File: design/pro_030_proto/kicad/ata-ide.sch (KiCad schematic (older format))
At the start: 31 parts, among them J1 Conn_02x32_Odd_Even, J2 Conn_02x20_Odd_Even, J3 Conn_02x22_Odd_Even, Q1 2N2907, U1 16V8, U2 ATF750, U3 74HCT241, U4 74HCT245, U5 74HCT245

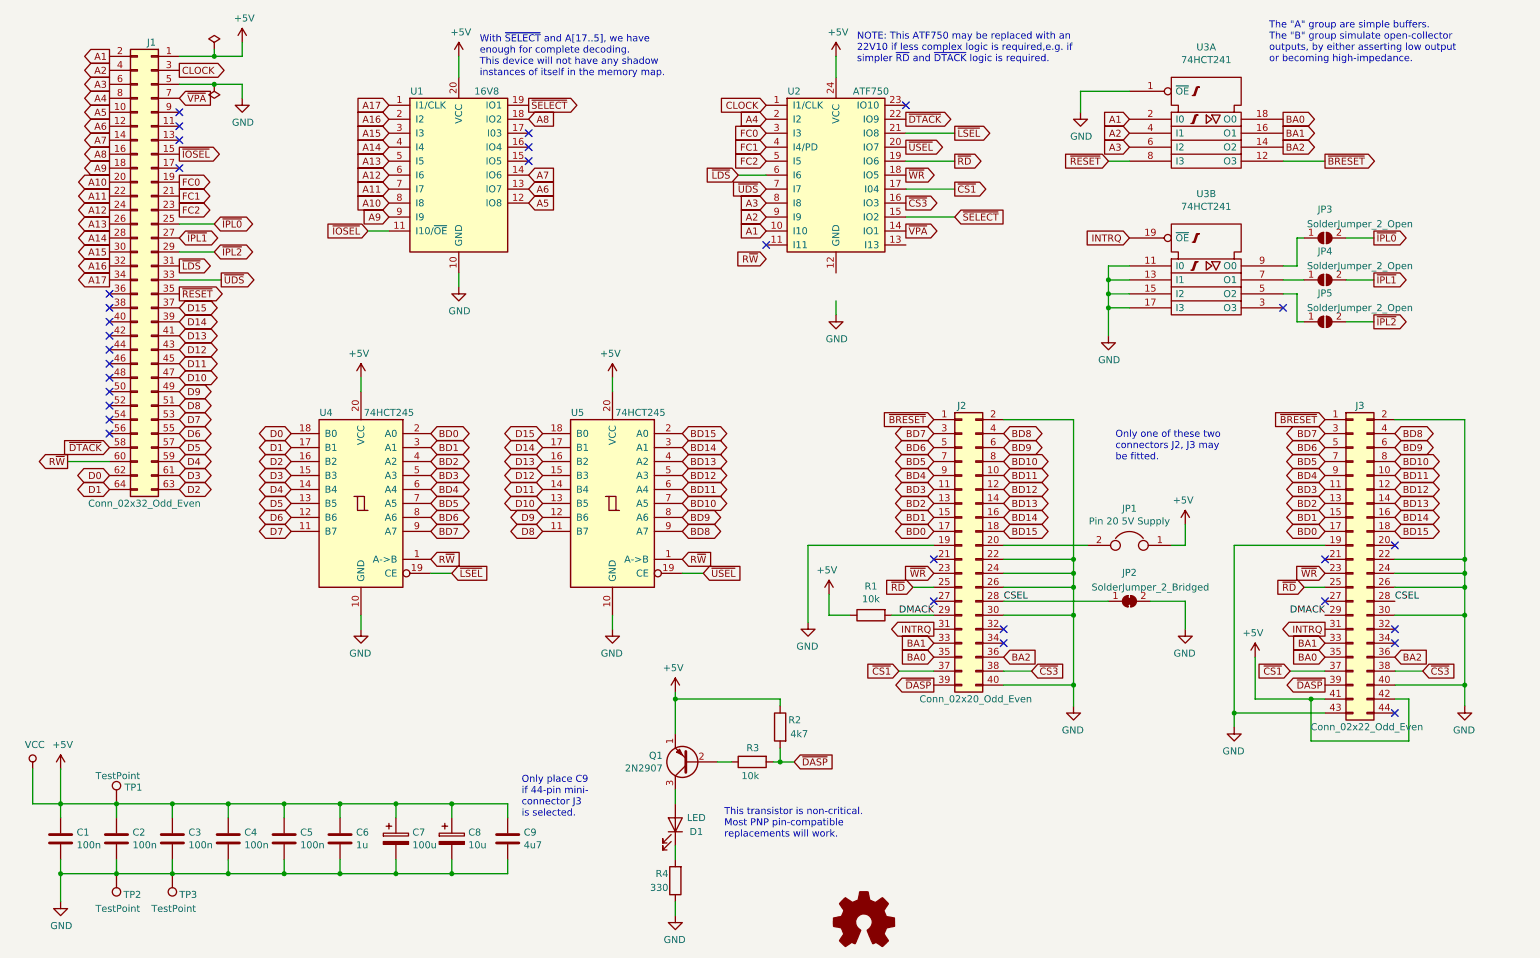
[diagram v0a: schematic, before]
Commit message: Layout for ATA, plus fixes
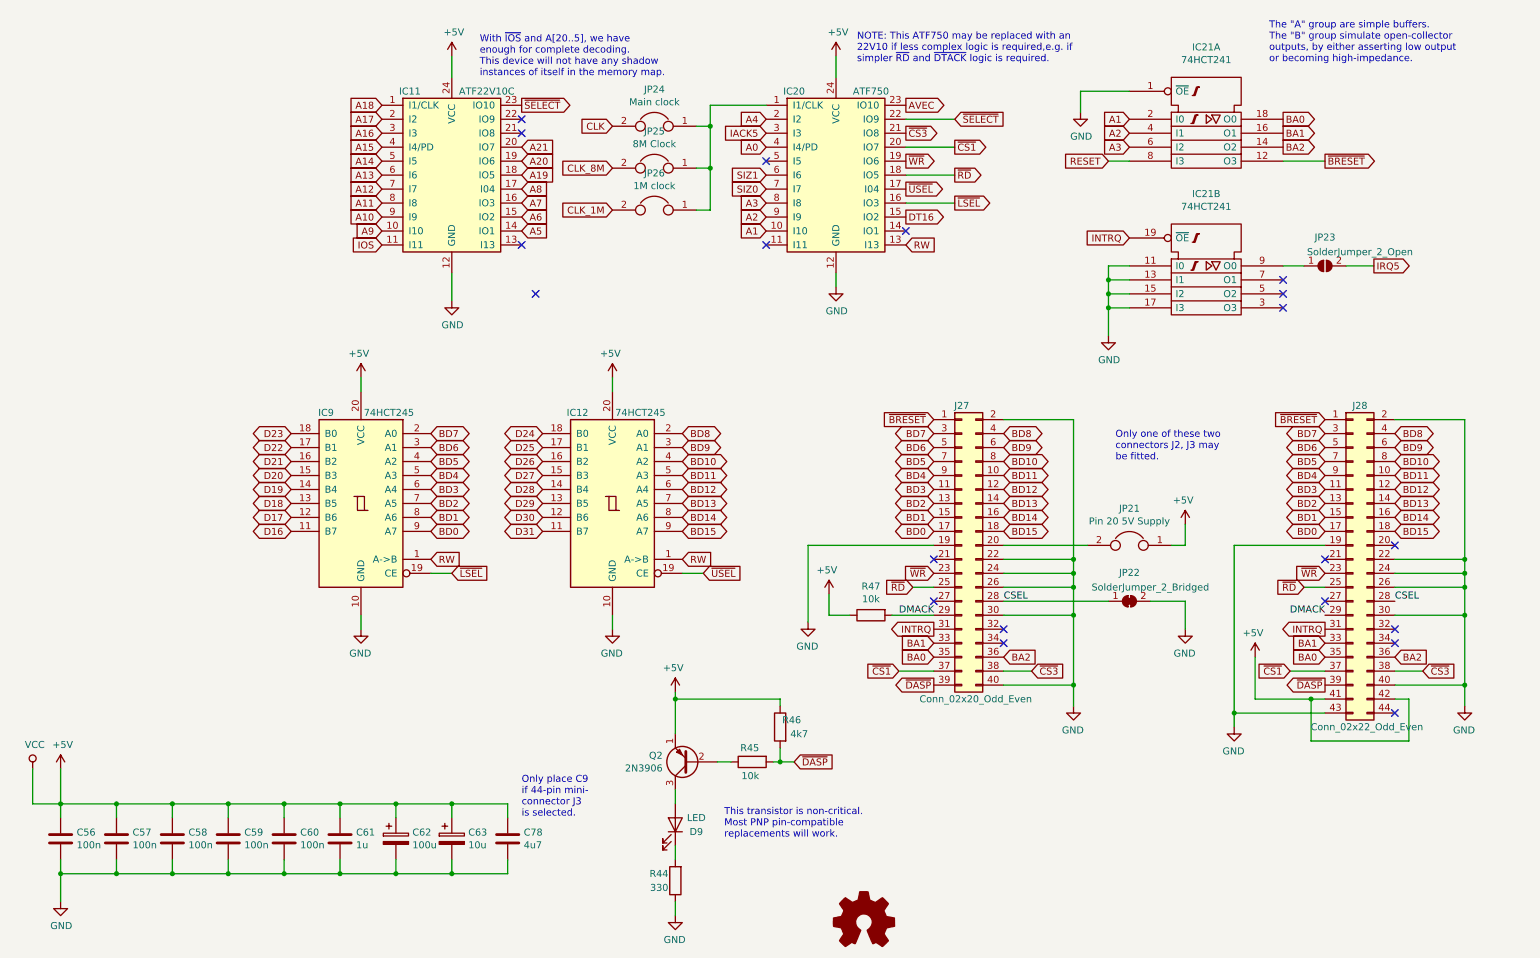
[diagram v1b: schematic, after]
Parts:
- removed J1: Conn_02x32_Odd_Even, Connector_PinHeader_2.54mm:PinHeader_2x32_P2.54mm_Vertical, symbol Connector_Generic:Conn_02x32_Odd_Even
- removed JP4, JP5: SolderJumper_2_Open, Jumper:SolderJumper-2_P1.3mm_Open_Pad1.0x1.5mm, symbol Jumper:SolderJumper_2_Open
- removed TP1, TP2, TP3: TestPoint, Measurement_Points:Measurement_Point_Round-TH_Big, symbol Connector:TestPoint
- removed U1: 16V8, Housings_DIP:DIP-20_W7.62mm_Socket_LongPads, symbol Logic_Programmable:GAL16V8
- added IC11: ATF22V10C, Package_DIP:DIP-24_W7.62mm_Socket_LongPads, symbol rosco_m68k:GAL22V10
- added JP24: Main clock, Connector_PinHeader_2.54mm:PinHeader_1x02_P2.54mm_Vertical, symbol Device:Jumper
- added JP25: 8M Clock, Connector_PinHeader_2.54mm:PinHeader_1x02_P2.54mm_Vertical, symbol Device:Jumper
- added JP26: 1M clock, Connector_PinHeader_2.54mm:PinHeader_1x02_P2.54mm_Vertical, symbol Device:Jumper
- C56: renamed from C1; footprint Capacitors_THT:C_Rect_L4.0mm_W2.5mm_P2.50mm -> Capacitor_THT:C_Rect_L4.0mm_W2.5mm_P2.50mm
- C57: renamed from C2; footprint Capacitors_THT:C_Rect_L4.0mm_W2.5mm_P2.50mm -> Capacitor_THT:C_Rect_L4.0mm_W2.5mm_P2.50mm
- C58: renamed from C3; footprint Capacitors_THT:C_Rect_L4.0mm_W2.5mm_P2.50mm -> Capacitor_THT:C_Rect_L4.0mm_W2.5mm_P2.50mm
- C59: renamed from C4; footprint Capacitors_THT:C_Rect_L4.0mm_W2.5mm_P2.50mm -> Capacitor_THT:C_Rect_L4.0mm_W2.5mm_P2.50mm
- C60: renamed from C5; footprint Capacitors_THT:C_Rect_L4.0mm_W2.5mm_P2.50mm -> Capacitor_THT:C_Rect_L4.0mm_W2.5mm_P2.50mm
- C61: renamed from C6; footprint Capacitors_THT:C_Rect_L7.0mm_W4.5mm_P5.00mm -> Capacitor_THT:C_Rect_L7.0mm_W4.5mm_P5.00mm
- C62: renamed from C7; footprint Capacitors_THT:CP_Radial_D8.0mm_P2.50mm -> Capacitor_THT:CP_Radial_D8.0mm_P2.50mm
- C63: renamed from C8; footprint Capacitors_THT:CP_Radial_D8.0mm_P2.50mm -> Capacitor_THT:CP_Radial_D8.0mm_P2.50mm
- C78: renamed from C9; footprint Capacitors_THT:C_Rect_L7.0mm_W4.5mm_P5.00mm -> Capacitor_THT:C_Rect_L7.0mm_W4.5mm_P5.00mm
- D9: renamed from D1; footprint LEDs:LED_D5.0mm -> LED_THT:LED_D3.0mm
- JP21: renamed from JP1; footprint Connector_PinHeader_2.00mm:PinHeader_1x02_P2.00mm_Vertical -> Connector_PinHeader_2.54mm:PinHeader_1x02_P2.54mm_Vertical
- Q2: renamed from Q1; value 2N2907 -> 2N3906; footprint Package_TO_SOT_THT:TO-18-3 -> Package_TO_SOT_THT:TO-92_HandSolder
- R44: renamed from R4; footprint Resistors_THT:R_Axial_DIN0207_L6.3mm_D2.5mm_P10.16mm_Horizontal -> rosco_m68k:R-0207_10
- R45: renamed from R3; footprint Resistors_THT:R_Axial_DIN0207_L6.3mm_D2.5mm_P10.16mm_Horizontal -> rosco_m68k:R-0207_10
- R46: renamed from R2; footprint Resistors_THT:R_Axial_DIN0207_L6.3mm_D2.5mm_P10.16mm_Horizontal -> rosco_m68k:R-0207_10
- R47: renamed from R1; footprint Resistors_THT:R_Axial_DIN0207_L6.3mm_D2.5mm_P10.16mm_Horizontal -> rosco_m68k:R-0207_10
- renumbered U5 to IC12, U2 to IC20, U3 to IC21, U4 to IC9, J2 to J27, J3 to J28, JP2 to JP22, JP3 to JP23
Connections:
- net R~W~ is gone; now on net RW: IC12.1 (A->B), IC9.1 (A->B)
- net ~DTACK~ is gone; now on net ~SELECT~: IC20.22 (IO9)
- net +5V: now also IC11.24 (VCC)
- net A10: now also IC11.9 (I9)
- net A11: now also IC11.8 (I8)
- net A12: now also IC11.7 (I7)
- net A13: now also IC11.6 (I6)
- net A14: now also IC11.5 (I5)
- net A15: now also IC11.4 (I4/PD)
- net A16: now also IC11.3 (I3)
- net A17: now also IC11.2 (I2)
- net A5: now also IC11.14 (IO1)
- net A6: now also IC11.15 (IO2)
- net A7: now also IC11.16 (IO3)
- net A8: now also IC11.17 (I04)
- net A9: now also IC11.10 (I10)
- net BD0: now also IC9.9 (A7); no longer IC9.2 (A0)
- net BD1: now also IC9.8 (A6); no longer IC9.3 (A1)
- net BD10: now also IC12.4 (A2); no longer IC12.7 (A5)
- net BD11: now also IC12.5 (A3); no longer IC12.6 (A4)
- net BD12: now also IC12.6 (A4); no longer IC12.5 (A3)
- net BD13: now also IC12.7 (A5); no longer IC12.4 (A2)
- net BD14: now also IC12.8 (A6); no longer IC12.3 (A1)
- net BD15: now also IC12.9 (A7); no longer IC12.2 (A0)
- net BD2: now also IC9.7 (A5); no longer IC9.4 (A2)
- net BD3: now also IC9.6 (A4); no longer IC9.5 (A3)
- net BD4: now also IC9.5 (A3); no longer IC9.6 (A4)
- net BD5: now also IC9.4 (A2); no longer IC9.7 (A5)
- net BD6: now also IC9.3 (A1); no longer IC9.8 (A6)
- net BD7: now also IC9.2 (A0); no longer IC9.9 (A7)
- net BD8: now also IC12.2 (A0); no longer IC12.9 (A7)
- net BD9: now also IC12.3 (A1); no longer IC12.8 (A6)
- net GND: now also IC20.12 (GND), IC11.12 (GND)
- net ~CS1~: now also IC20.20 (IO7); no longer IC20.17 (I04)
- net ~CS3~: now also IC20.21 (IO8); no longer IC20.16 (IO3)
- net ~LSEL~: now also IC20.16 (IO3); no longer IC20.21 (IO8)
- net ~RD~: now also IC20.18 (IO5); no longer IC20.19 (IO6)
- net ~SELECT~: now also IC11.23 (IO10); no longer IC20.15 (IO2)
- net ~USEL~: now also IC20.17 (I04); no longer IC20.20 (IO7)
- net ~WR~: now also IC20.19 (IO6); no longer IC20.18 (IO5)
- net RW: now reaches IC20.13 (I13)
- net AVEC: now reaches IC20.23 (IO10)
- net CLOCK: no longer names the net of IC20.1 (I1/CLK)
- net CLOCK: now also JP24.1, JP25.1, JP26.1
- net D0 renamed D23
- net D1 renamed D22
- net D10 renamed D29
- net D11 renamed D28
- net D12 renamed D27
- net D13 renamed D26
- net D14 renamed D25
- net D15 renamed D24
- net D2 renamed D21
- net D3 renamed D20
- net D4 renamed D19
- net D5 renamed D18
- net D6 renamed D17
- net D7 renamed D16
- net D8 renamed D31
- net D9 renamed D30
- net FC0 renamed IACK5
- net FC1 renamed A0
- net FC2: no longer names the net of IC20.5 (I5)
- net ~IPL0~ renamed IRQ5
- net ~LDS~ renamed SIZ1
- net ~RESET~ renamed RESET
- net ~UDS~ renamed SIZ0
- net ~VPA~: no longer names the net of IC20.14 (IO1)
- new net A18: IC11.1 (I1/CLK)
- new net A19: IC11.18 (IO5)
- new net A20: IC11.19 (IO6)
- new net A21: IC11.20 (IO7)
- new net CLK: JP24.2
- new net CLK_1M: JP26.2
- new net CLK_8M: JP25.2
- new net DT16: IC20.15 (IO2)
- new net IOS: IC11.11 (I11)
- no-connect marks 31 -> 20
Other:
- note added: "With ~IOS~ and A[20..5], we have\nenough for complete decoding.\nThis device will not have any shadow\ninstances of itself in the memory map."
- note removed: "With ~SELECT~ and A[17..5], we have\nenough for complete decoding.\nThis device will not have any shadow\ninstances of itself in the memory map."
- moved on the sheet: JP23

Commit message: Tidy up a bit
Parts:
- JP23: footprint Jumper:SolderJumper-2_P1.3mm_Open_Pad1.0x1.5mm -> Jumper:SolderJumper-2_P1.3mm_Bridged_Pad1.0x1.5mm; symbol Jumper:SolderJumper_2_Open -> Jumper:SolderJumper_2_Bridged
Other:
- note added: "Only place C78\nif 44-pin mini-\nconnector J3\nis selected."
- note removed: "Only place C9\nif 44-pin mini-\nconnector J3\nis selected."
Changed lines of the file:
@@
 	650  6650 850  6650
 $Comp
-L Jumper:SolderJumper_2_Open JP23
+L Jumper:SolderJumper_2_Bridged JP23
 U 1 1 6064DE34
 P 9900 2800
 F 0 "JP23" H 9900 3005 50  0000 C CNN
 F 1 "SolderJumper_2_Open" H 10150 2900 50  0000 C CNN
-F 2 "Jumper:SolderJumper-2_P1.3mm_Open_Pad1.0x1.5mm" H 9900 2800 50  0001 C CNN
+F 2 "Jumper:SolderJumper-2_P1.3mm_Bridged_Pad1.0x1.5mm" H 9900 2800 50  0001 C CNN
 F 3 "~" H 9900 2800 50  0001 C CNN
 	1    9900 2800
@@
 Connection ~ 3650 7150
 Text Notes 4150 6750 0    50   ~ 0
-Only place C9\nif 44-pin mini-\nconnector J3\nis selected.
+Only place C78\nif 44-pin mini-\nconnector J3\nis selected.
 Wire Wire Line
 	6900 2350 7250 2350

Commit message: Add panel header block
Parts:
- added J26: IDE_LED, Connector_PinHeader_2.54mm:PinHeader_2x01_P2.54mm_Vertical, symbol Connector_Generic:Conn_02x01
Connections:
- net at D9.1 (K), R44.2: now also J26.2 (Pin_2)
- net at D9.2 (A), Q2.3 (C): now also J26.1 (Pin_1)
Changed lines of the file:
@@
 	4050 7150 3650 7150
 Connection ~ 3650 7150
-Text Notes 4150 6750 0    50   ~ 0
+Text Notes 3550 6450 0    50   ~ 0
 Only place C78\nif 44-pin mini-\nconnector J3\nis selected.
 Wire Wire Line
@@
 NoConn ~ 4150 2650
 NoConn ~ 4250 3000
+$Comp
+L Connector_Generic:Conn_02x01 J?
+U 1 1 61E8C30F
+P 4800 6750
+AR Path="/60FC48A0/61E8C30F" Ref="J?"  Part="1"
+AR Path="/61B3F22F/61E8C30F" Ref="J26"  Part="1"
+F 0 "J26" H 4850 6967 50  0000 C CNN
+F 1 "IDE_LED" H 4850 6876 50  0000 C CNN
+F 2 "Connector_PinHeader_2.54mm:PinHeader_2x01_P2.54mm_Vertical" H 4800 6750 50  0001 C CNN
+F 3 "~" H 4800 6750 50  0001 C CNN
+	1    4800 6750
+	0    1    1    0
+$EndComp
+Wire Wire Line
+	4800 7050 5250 7050
+Connection ~ 5250 7050
+Wire Wire Line
+	4800 6550 5250 6550
+Connection ~ 5250 6550
 $EndSCHEMATC

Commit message: More tidy up & swap layers
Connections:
- net JPIRQ5: now reaches IC21.9 (O0), JP23.1 (A)
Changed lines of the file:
@@
 	4800 6550 5250 6550
 Connection ~ 5250 6550
+Text Label 9600 2800 0    50   ~ 0
+JPIRQ5
 $EndSCHEMATC

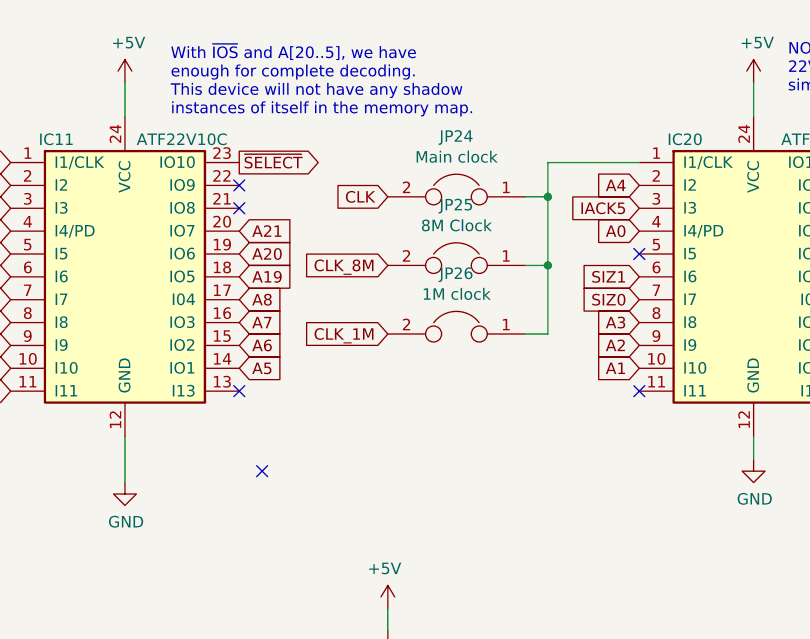
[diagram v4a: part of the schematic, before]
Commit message: Add new Xosera DTACK stretch GAL
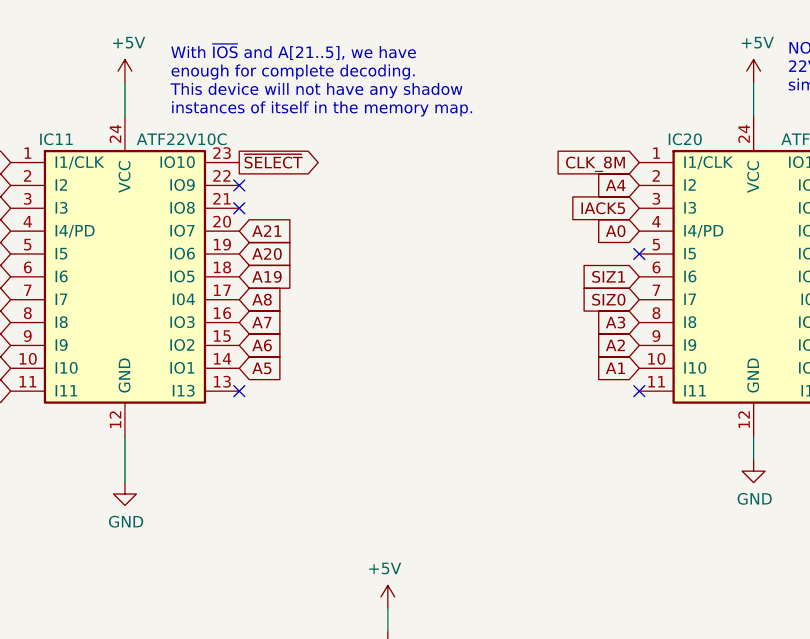
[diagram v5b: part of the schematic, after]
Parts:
- removed JP24: Main clock, Connector_PinHeader_2.54mm:PinHeader_1x02_P2.54mm_Vertical, symbol Device:Jumper
- removed JP25: 8M Clock, Connector_PinHeader_2.54mm:PinHeader_1x02_P2.54mm_Vertical, symbol Device:Jumper
- removed JP26: 1M clock, Connector_PinHeader_2.54mm:PinHeader_1x02_P2.54mm_Vertical, symbol Device:Jumper
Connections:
- net CLK_8M: now also IC20.1 (I1/CLK)
- no-connect marks 20 -> 19
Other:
- note added: "With ~IOS~ and A[21..5], we have\nenough for complete decoding.\nThis device will not have any shadow\ninstances of itself in the memory map."
- note removed: "With ~IOS~ and A[20..5], we have\nenough for complete decoding.\nThis device will not have any shadow\ninstances of itself in the memory map."
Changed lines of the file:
@@
 ~LSEL~
 Text Notes 3850 1450 0    50   ~ 0
-With ~IOS~ and A[20..5], we have\nenough for complete decoding.\nThis device will not have any shadow\ninstances of itself in the memory map.
+With ~IOS~ and A[21..5], we have\nenough for complete decoding.\nThis device will not have any shadow\ninstances of itself in the memory map.
 $Comp
 L Graphic:Logo_Open_Hardware_Small #LOGO1
@@
 Wire Wire Line
 	9600 2800 9750 2800
-$Comp
-L Device:Jumper JP24
-U 1 1 61B11C1E
-P 5100 1800
-F 0 "JP24" H 5100 2064 50  0000 C CNN
-F 1 "Main clock" H 5100 1973 50  0000 C CNN
-F 2 "Connector_PinHeader_2.54mm:PinHeader_1x02_P2.54mm_Vertical" H 5100 1800 50  0001 C CNN
-F 3 "~" H 5100 1800 50  0001 C CNN
-	1    5100 1800
-	-1   0    0    -1
-$EndComp
-$Comp
-L Device:Jumper JP25
-U 1 1 61B162C3
-P 5100 2100
-F 0 "JP25" H 5100 2364 50  0000 C CNN
-F 1 "8M Clock" H 5100 2273 50  0000 C CNN
-F 2 "Connector_PinHeader_2.54mm:PinHeader_1x02_P2.54mm_Vertical" H 5100 2100 50  0001 C CNN
-F 3 "~" H 5100 2100 50  0001 C CNN
-	1    5100 2100
-	-1   0    0    -1
-$EndComp
-$Comp
-L Device:Jumper JP26
-U 1 1 61B1AA97
-P 5100 2400
-F 0 "JP26" H 5100 2664 50  0000 C CNN
-F 1 "1M clock" H 5100 2573 50  0000 C CNN
-F 2 "Connector_PinHeader_2.54mm:PinHeader_1x02_P2.54mm_Vertical" H 5100 2400 50  0001 C CNN
-F 3 "~" H 5100 2400 50  0001 C CNN
-	1    5100 2400
-	-1   0    0    -1
-$EndComp
-Wire Wire Line
-	5400 2400 5500 2400
-Wire Wire Line
-	5400 1800 5500 1800
-Wire Wire Line
-	5400 2100 5500 2100
-Text GLabel 4800 1800 0    50   Input ~ 0
-CLK
-Text GLabel 4800 2100 0    50   Input ~ 0
+Text GLabel 5900 1650 0    50   Input ~ 0
 CLK_8M
-Text GLabel 4800 2400 0    50   Input ~ 0
-CLK_1M
 Text GLabel 5900 2250 0    50   Input ~ 0
 SIZ0
@@
 Wire Wire Line
 	3650 2850 3650 3050
-Connection ~ 5500 2100
-Wire Wire Line
-	5500 1800 5500 2100
-Wire Wire Line
-	5500 2100 5500 2400
-Wire Wire Line
-	5900 1650 5500 1650
-Wire Wire Line
-	5500 1650 5500 1800
-Connection ~ 5500 1800
 NoConn ~ 4150 2650
-NoConn ~ 4250 3000
 $Comp
 L Connector_Generic:Conn_02x01 J?
